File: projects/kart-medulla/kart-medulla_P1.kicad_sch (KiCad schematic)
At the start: 55 parts, among them CN1 1990012, CN10 1990012, CN2 1990012, CN3 1990012, CN4 1990012, CN5 1990012, CN6 1990012, CN7 1990012, CN8 1990012, CN9 1990012, Q3 IRLZ44NPBF, Q4 BSS123_C5184436, U1 LM358DR, U13 MCP4922-E/SL, U14 MAX4660EUA+T, U19 L7805CDT_C20611927, U23 SSW-122-01-T-D, U24 SSW-122-01-T-S, U25 PCF8574T/3,518, U5 SN74LVC3G17DCTR

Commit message: pcb in progress
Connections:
- net +3V3: now also CN1.1
- net CMD_STEER_DIR__3V3: now also U23.19, U23.20; no longer U24.9
- net EXP_P1: now also CN3.3; no longer CN3.2
- net EXP_P2: now also CN3.2; no longer CN3.3
- net GND: no longer CN1.1
- net PEDAL_ACC__0_5V: now also CN6.2; no longer CN6.1
- net PEDAL_BRAKE__0_5V: now also CN6.1; no longer CN6.2
- net SDC_NOT_EMERGENCY__3V3: now also U23.21, U23.22; no longer U24.13
- no-connect marks 26 -> 24
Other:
- note added: "BLOCKED - RX0 (GPIO44, UART0), dev-board USB-UART bridge"
- note added: "BLOCKED - TX0 (GPIO43, UART0), dev-board USB-UART bridge"
- note added: "BLOCKED: on-board LED of ESP32-S3 pcb, GPIO48"
- note added: "HOLD (BOOT strap, GPIO 0)"
- note added: "HOLD (strap, flash/boot risk)"
- note added: "HOLD - Octal-PSRAM pin on N8R8"
- note added: "HOLD - unconstrained GPIO 39, kept free for future expansion"
- note added: "HOLD for CAN_RX"
- note added: "HOLD for CAN_TX"
- note added: "free"
- note removed: "RESERVE - RX0 (GPIO44, UART0), dev-board USB-UART bridge"
- note removed: "RESERVE - TX0 (GPIO43, UART0), dev-board USB-UART bridge"
- note removed: "RESERVE: on-board LED of ESP32-S3 pcb, GPIO48"
- note removed: "SDC_ENABLE — orphan, expected from external module"
- note removed: "SPARE - Octal-PSRAM pin on N8R8"
- note removed: "SPARE for CAN_RX"
- note removed: "SPARE for CAN_TX"
- note removed: "STRAP PIN (flash/boot risk)"
- note removed: "UART1 RX1 - free (usbc uses UART0)"
- note removed: "UART1 TX1 - free (usbc uses UART0)"

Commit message: refilled update
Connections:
- net EXP_P1: now also CN3.1; no longer CN3.3
- net EXP_P3: now also CN3.3; no longer CN3.1
- net REVERSE_WIRE: now also CN4.3; no longer CN4.1
- net SCL__I2C: now also CN4.1; no longer CN4.3
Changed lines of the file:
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@@
 		)
 	)
-	(label "EXP_P1"
+	(label "EXP_P3"
 		(at 45.72 85.09 0)
 		(effects
@@
 		)
 	)
-	(label "REVERSE_WIRE"
+	(label "SCL__I2C"
 		(at 100.33 46.99 0)
 		(effects
@@
 		)
 	)
-	(label "SCL__I2C"
+	(label "REVERSE_WIRE"
 		(at 100.33 52.07 0)
 		(effects
@@
 		)
 	)
-	(label "EXP_P3"
+	(label "EXP_P1"
 		(at 45.72 80.01 0)
 		(effects

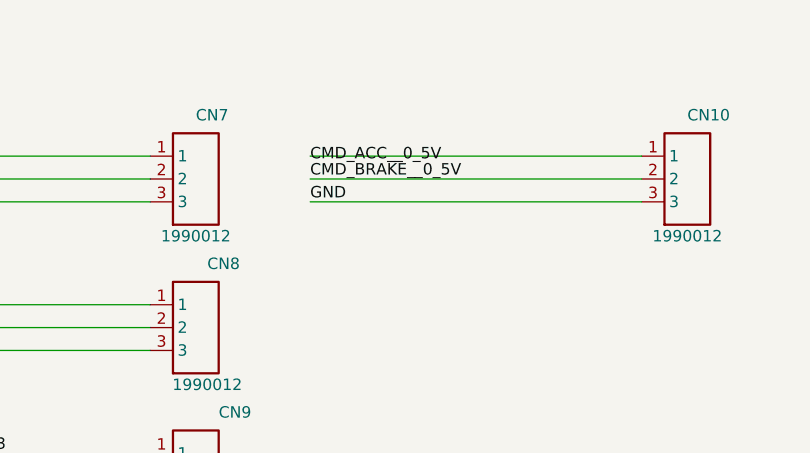
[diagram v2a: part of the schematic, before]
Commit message: medulla: route the valve command out at 0-10V; restore the DAC->amp copper
Schematic: one label, at (218.44, 48.26) on CN10 pin 2's stub, renamed
CMD_BRAKE__0_5V -> CMD_BRAKE__0_10V. Every connection in this chain is a label on
a stub, so nothing else moved. Netlist now splits correctly: CMD_BRAKE__0_5V =
U13.10 + U1.3, CMD_BRAKE__0_10V = CN10.2 + R19.2 + U1.1. ERC 0 violations.

PCB: CN10 pad 2's net updated, then routed to the 0-10V net on F.Cu - 45 deg from
(74.5, 90.9999) to (81.0727, 97.5726), east to (87.0, 97.5726), 0.6/0.3 via down
onto the existing B.Cu stub between U1.1 and R19.2. F.Cu because that corridor is
empty on the front layer while B.Cu is not. Clears CN10.1's through-hole pad by
~0.81 mm against a 0.254 mm rule.

Also restored: U13.10 -> U1.3, the DAC-to-amplifier copper. Six of the seven
CMD_BRAKE__0_5V segments had been deleted in KiCad, leaving that connection
unrouted; DRC flagged it as a missing connection between U1.3 and U13.10. Put the
original geometry back, since the surrounding layout was designed around it.

Zones refilled via pcbnew (kicad-cli does not refill, which is why the first DRC
run showed 6 stale-pour clearance errors). Final: DRC 0 violations, 0 unconnected.
The 5 remaining parity warnings are byte-identical to the previous commit's.
pcbnew's save rewrites the file canonically, hence the large diff; object counts
verified unchanged except the one new via.
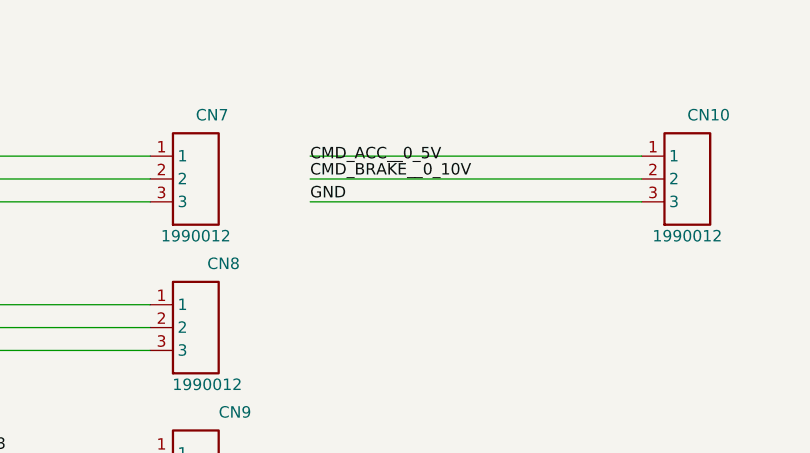
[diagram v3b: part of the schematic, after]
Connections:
- net CMD_BRAKE__0_10V: now also CN10.2
- net CMD_BRAKE__0_5V: no longer CN10.2
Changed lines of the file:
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@@
 		)
 	)
-	(label "CMD_BRAKE__0_5V"
+	(label "CMD_BRAKE__0_10V"
 		(at 218.44 48.26 0)
 		(effects

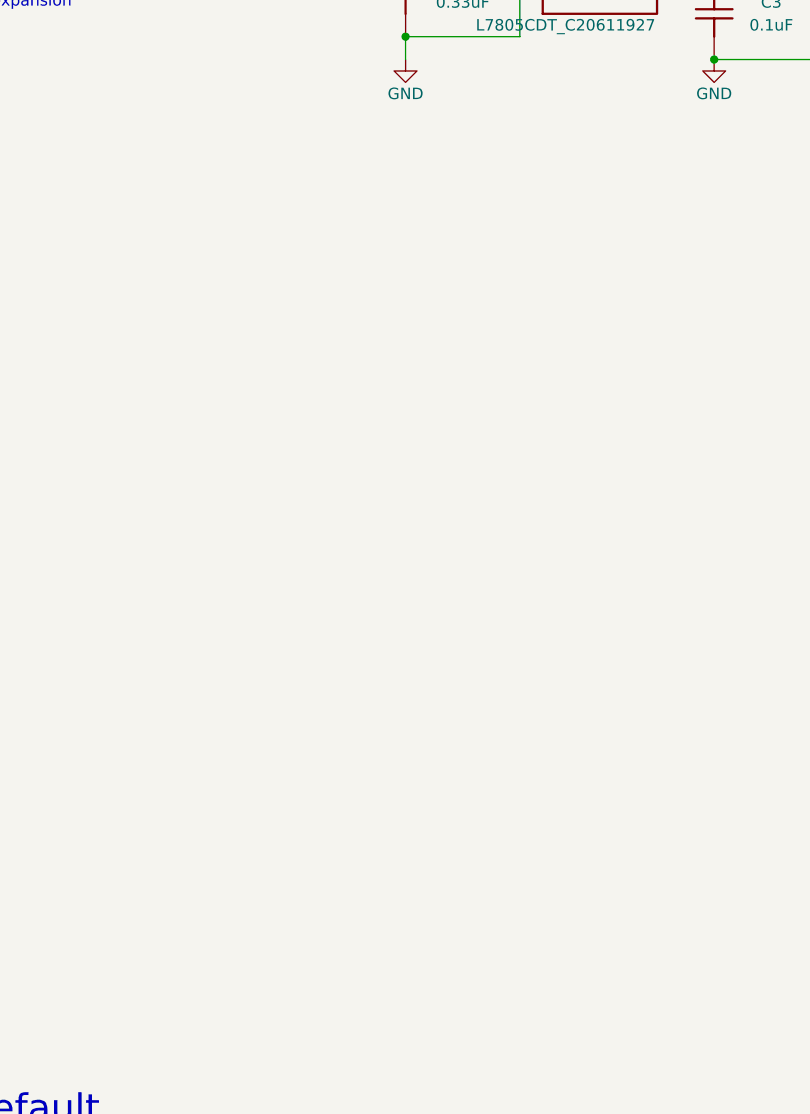
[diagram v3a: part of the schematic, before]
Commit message: add the seven ADC filter caps, C7-C13
100 nF on each analog input's divider node: C7 PEDAL_ACC, C8 PEDAL_BRAKE, C9 HYDRAULIC_1,
C10 HYDRAULIC_2, C11 PRESSURE_1, C12 PRESSURE_2, C13 PRESSURE_3. The task list had asked
for these since 2026-05 and the board had none - its only six capacitors are all on power
rails.

Value checks out across all three divider impedances: 5.0k source on the pedals gives a
318 Hz corner, 1.32k on hydraulics 1.2 kHz, 6.67k on the pressures 239 Hz - all far above
the signals and far below anything the ADC tracks. The bigger reason is the ESP32-S3 SAR
ADC charging its sampling capacitor from a 6.67k source; the cap is the reservoir that
feeds it.

Direct file edit, no MCP writes - the guard script reported kicad-mcp-pro running. Verified
by ERC (0 violations), a fresh netlist export showing all seven on their intended nets with
GND on the other pin, and an SVG render. The render caught a text collision the netlist
could not: at 7.62 mm spacing each value label landed on the next reference designator.
Respaced to 12.7 mm.

Left for the PCB: place each cap at the ESP32 ADC pin, not at its divider.
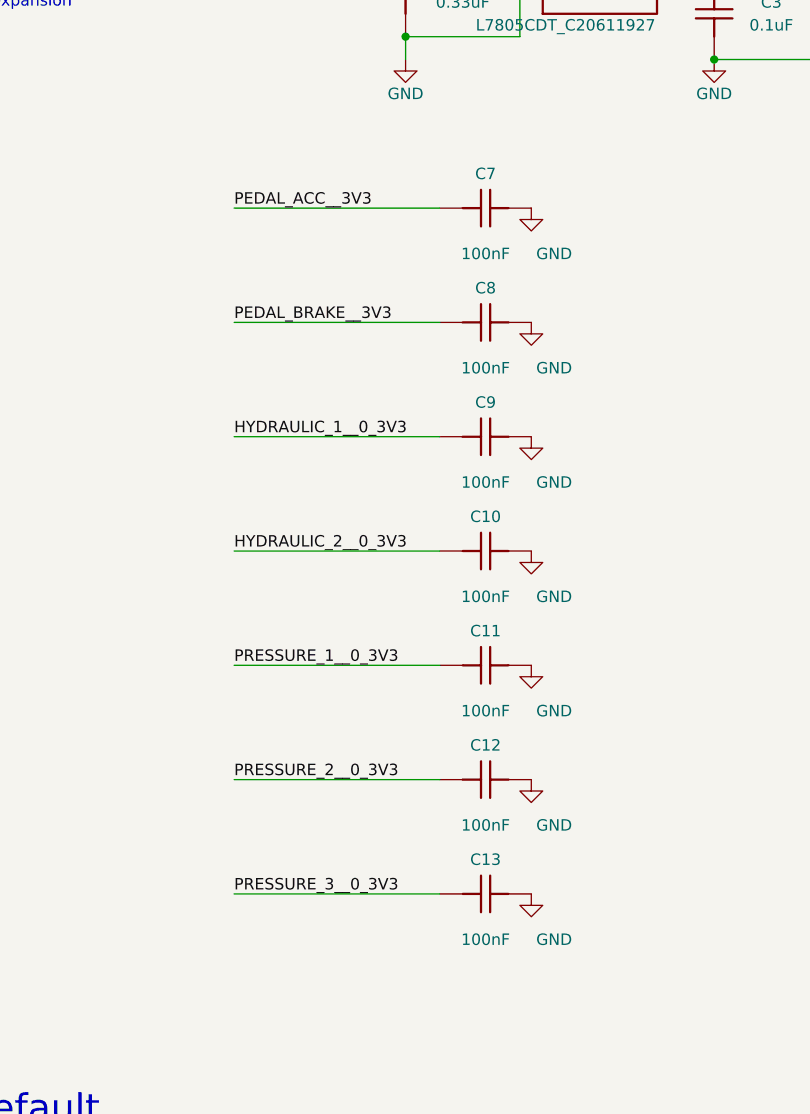
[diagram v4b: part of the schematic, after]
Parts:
- added C10, C11, C12, C13, C7, C8, C9: 100nF, kart-medulla:C0603, symbol kart-medulla:CAP
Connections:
- net GND: now also C10.1, C11.1, C12.1, C13.1, C7.1, C8.1, C9.1
- net HYDRAULIC_1__0_3V3: now also C9.2
- net HYDRAULIC_2__0_3V3: now also C10.2
- net PEDAL_ACC__3V3: now also C7.2
- net PEDAL_BRAKE__3V3: now also C8.2
- net PRESSURE_1__0_3V3: now also C11.2
- net PRESSURE_2__0_3V3: now also C12.2
- net PRESSURE_3__0_3V3: now also C13.2

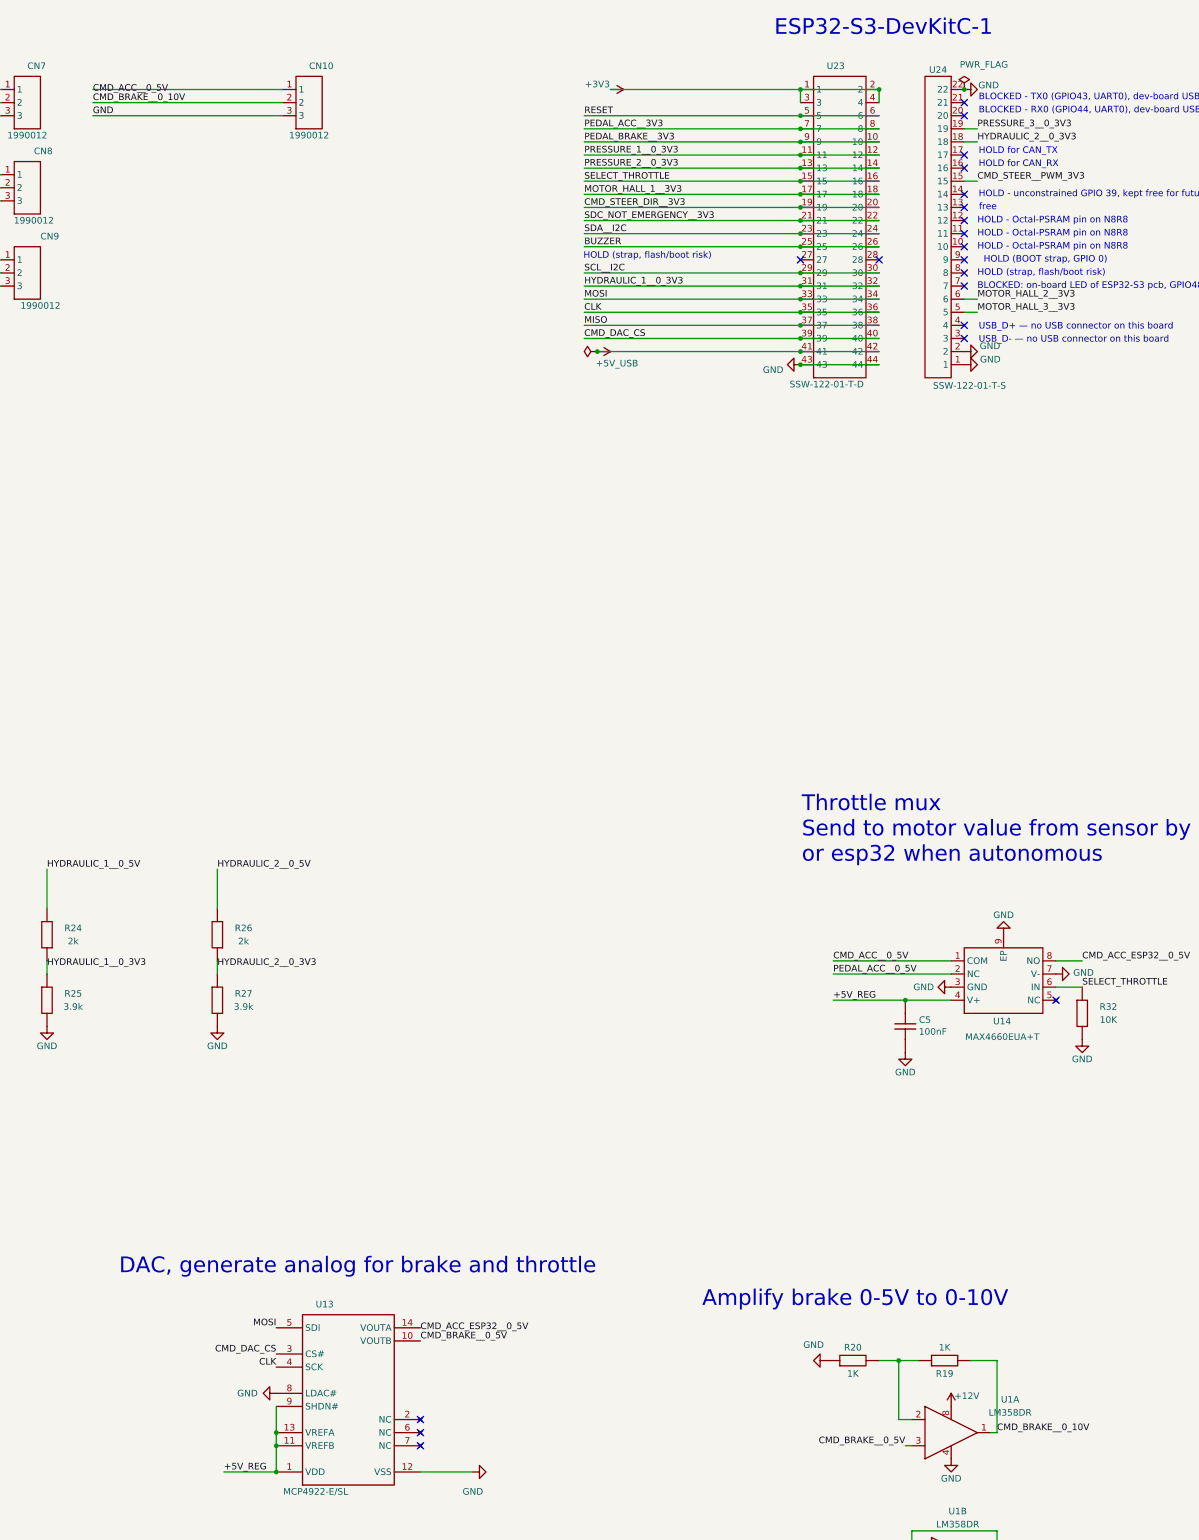
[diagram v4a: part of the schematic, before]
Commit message: rename CMD_BRAKE -> CMD_PRES; file the MCP4922 datasheet and close two open numbers
Net rename (task item 3): CMD_BRAKE__0_5V -> CMD_PRES_DAC__0_5V and CMD_BRAKE__0_10V ->
CMD_PRES__0_10V, following the throttle channel's internal-vs-exported pattern. CMD_PRES
because it is a pressure setpoint for a proportional regulator, not a brake-force command.
Applied to schematic (4), PCB (15) and both pinout docs so the two stay in parity. ERC 0
violations, DRC 0 violations, 0 unconnected. The one remaining CMD_BRAKE is under the
'Legacy: classic ESP32' heading and correct there.

MCP4922 datasheet filed (item 4). Output swing is 0.01 V to VDD-0.04 V typical, so full
scale on the 5 V rail is ~4.96 V - 0.8% short, or 9.92 V instead of 10.00 V after the x2.
That is ~0.08 bar on a 1 bar/volt valve, negligible beside the LM358's 1-2 V of lost
headroom, so the op-amp stays the binding limit. Accuracy is only guaranteed within 1 LSb
between 10 mV and VDD-40 mV.

Two firmware constraints follow from VREF being tied to VDD, neither implemented: GA=1 for
1x gain (GA=0 asks a 5 V part for 10 V), and BUF=0 for unbuffered VREF (buffered mode's
input range stops at VDD-0.040, and VREF here is VDD).

Over-voltage number (item 2): absolute max on any output is -0.3 V to VDD+0.3 V, so -0.3 to
+5.3 V, with output current capped at 25 mA. The valve runs on 24 V, so the old CN10.2
wiring exposed VOUTB to roughly 19 V over absolute maximum with nothing in the way.

Only item 1 is left and it needs a multimeter on the assembled board.
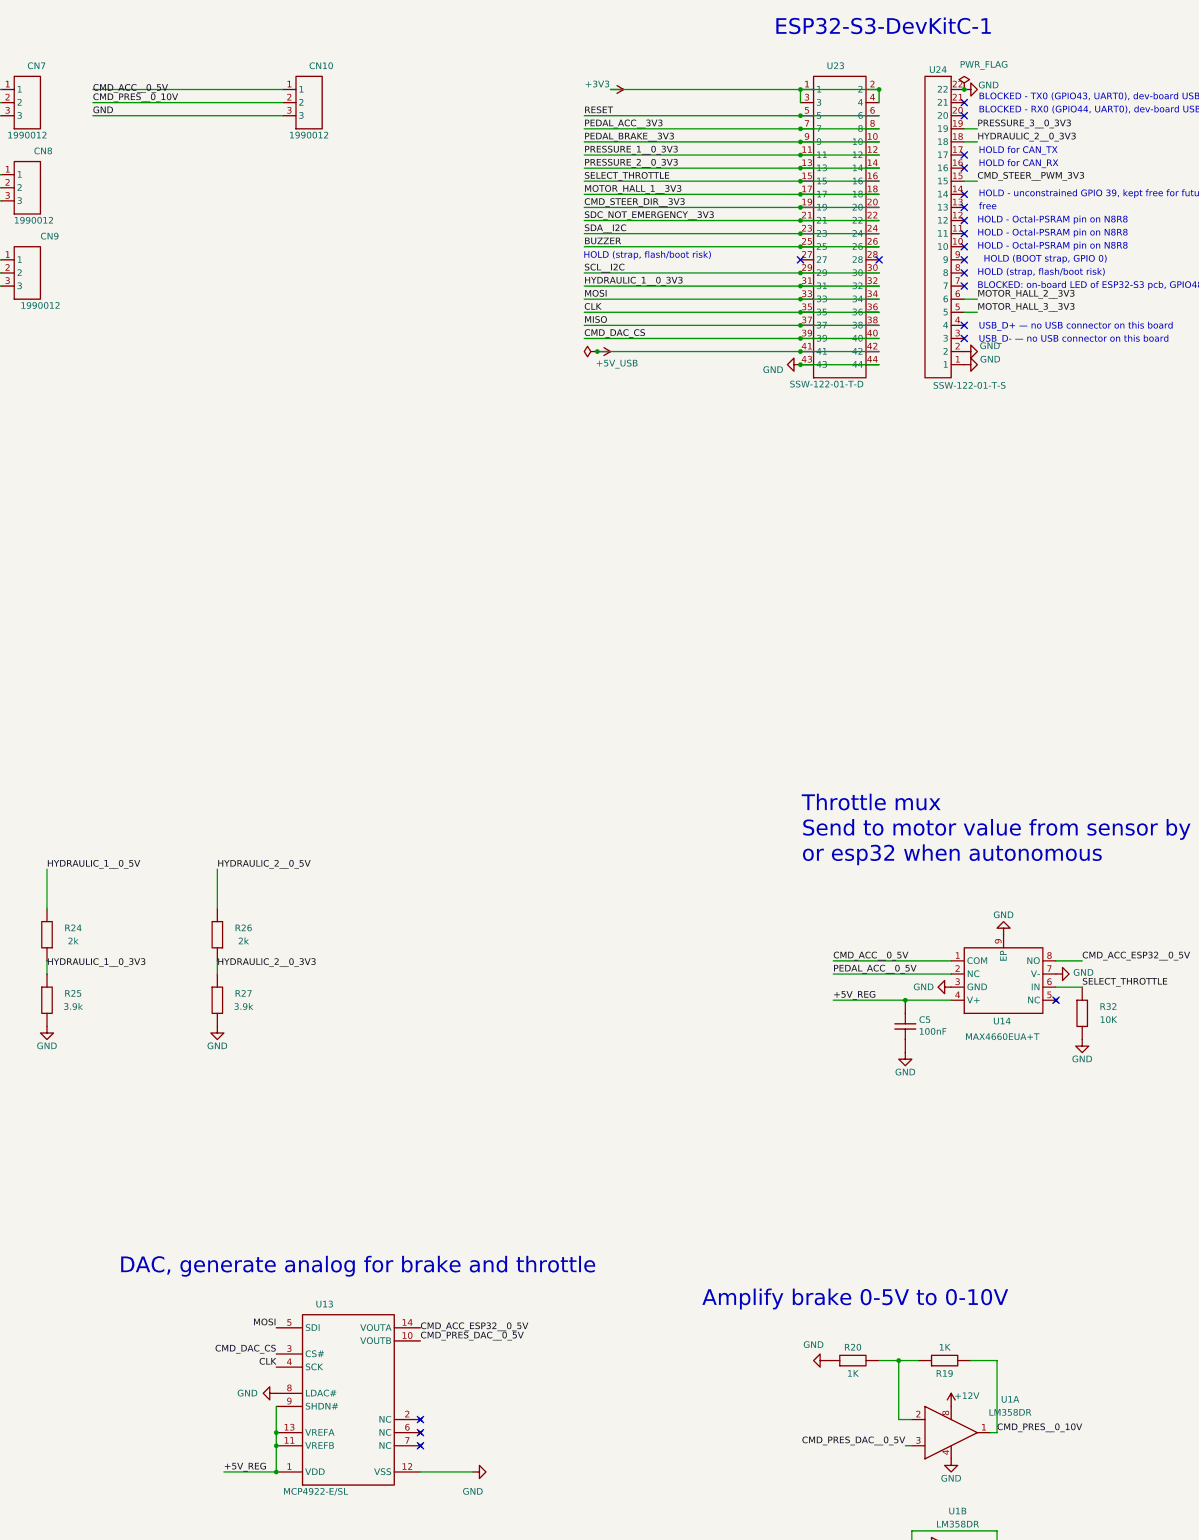
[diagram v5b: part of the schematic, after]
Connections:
- net CMD_BRAKE__0_10V renamed CMD_PRES__0_10V
- net CMD_BRAKE__0_5V renamed CMD_PRES_DAC__0_5V
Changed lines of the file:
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@@
 		)
 	)
-	(label "CMD_BRAKE__0_10V"
+	(label "CMD_PRES__0_10V"
 		(at 218.44 48.26 0)
 		(effects
@@
 		)
 	)
-	(label "CMD_BRAKE__0_10V"
+	(label "CMD_PRES__0_10V"
 		(at 393.7 306.07 0)
 		(effects
@@
 		)
 	)
-	(label "CMD_BRAKE__0_5V"
+	(label "CMD_PRES_DAC__0_5V"
 		(at 281.94 288.29 0)
 		(effects
@@
 		)
 	)
-	(label "CMD_BRAKE__0_5V"
+	(label "CMD_PRES_DAC__0_5V"
 		(at 375.92 308.61 180)
 		(effects

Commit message: fix three audit findings: U1 footprint field, U25 package, SMD/TH attributes
U1 (LM358): both units had an empty Footprint field, so the SOIC-8 existed only as a
PCB-side override and the BOM was wrong. Set on both.

U25: the symbol is PCF8574T/3,518 - NXP's /3 suffix is the narrow SO16 body, 3.9 mm - but
it was pointed at kart-medulla:SOIC-16_L10.3-W7.5-P1.27-LS10.3-BL, a wide-body land pattern
with pads at y=+/-4.7503 and 2.4 mm height, so the inner pad edge sits 3.55 mm from centre
against a 3.0 mm lead tip: 0.55 mm short on every lead. Retargeted to the KiCad stock
narrow pattern Package_SO:SOIC-16_3.9x9.9mm_P1.27mm. The PCB still carries the wide
footprint, so parity now reports that mismatch deliberately - applying it needs the local
re-route that the v2 re-layout will do anyway.

Footprint attributes: only 2 of 38 library footprints and 2 of 60 PCB footprints declared
smd or through_hole, so pick-and-place exported 1 placement out of the whole board.
Classified every footprint by its own pad types and set the attribute in both the library
and the PCB copies. The four standalone mechanical pads also get exclude_from_pos_files.
Export now yields 55 placements, 42 bottom and 13 top.

ERC 0 violations, DRC 0 violations, 0 unconnected.
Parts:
- U1: footprint (none) -> kart-medulla:SOIC-8_L5.0-W4.0-P1.27-LS6.0-BL
- U25: footprint kart-medulla:SOIC-16_L10.3-W7.5-P1.27-LS10.3-BL -> Package_SO:SOIC-16_3.9x9.9mm_P1.27mm
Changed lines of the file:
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@@
 			)
 		)
-		(property "Footprint" "kart-medulla:SOIC-16_L10.3-W7.5-P1.27-LS10.3-BL"
+		(property "Footprint" "Package_SO:SOIC-16_3.9x9.9mm_P1.27mm"
 			(at 486.41 217.17 0)
 			(hide yes)
@@
 			)
 		)
-		(property "Footprint" ""
+		(property "Footprint" "kart-medulla:SOIC-8_L5.0-W4.0-P1.27-LS6.0-BL"
 			(at 386.08 331.47 0)
 			(hide yes)
@@
 			)
 		)
-		(property "Footprint" ""
+		(property "Footprint" "kart-medulla:SOIC-8_L5.0-W4.0-P1.27-LS6.0-BL"
 			(at 384.81 306.07 0)
 			(hide yes)
